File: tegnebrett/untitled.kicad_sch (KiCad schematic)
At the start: 39 parts, among them U1 XC7A100T-2FTG256I

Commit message: feat: add FPGA footprint and add footprint to PCB
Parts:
- U1: footprint (none) -> tegnebrett_modules:fpga
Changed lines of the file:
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@@
 			)
 		)
-		(property "Footprint" ""
+		(property "Footprint" "tegnebrett_modules:fpga"
 			(at 204.47 85.09 0)
 			(effects

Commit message: feat: add footprint for each capacitor
It's all 0805, 1206 or 1210 hand soldering variants.
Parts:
- C1, C10, C11, C12, C13, C15, C16, C17, C18, C19, C21, C22, C23, C24, C26, C27, C28, C29, C3, C31, C32, C33, C34, C36, C37, C38, C39, C40, C41, C42, C43, C44, C45, C5, C7, C9: footprint (none) -> Capacitor_SMD:C_0805_2012Metric_Pad1.18x1.45mm_HandSolder
- C4: footprint (none) -> Capacitor_SMD:C_1210_3225Metric_Pad1.33x2.70mm_HandSolder
- C6: footprint (none) -> Capacitor_SMD:C_1206_3216Metric_Pad1.33x1.80mm_HandSolder
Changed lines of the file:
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@@
 			)
 		)
-		(property "Footprint" ""
+		(property "Footprint" "Capacitor_SMD:C_0805_2012Metric_Pad1.18x1.45mm_HandSolder"
 			(at 38.4048 86.36 0)
 			(effects
@@
 			)
 		)
-		(property "Footprint" ""
+		(property "Footprint" "Capacitor_SMD:C_0805_2012Metric_Pad1.18x1.45mm_HandSolder"
 			(at 59.3852 62.23 0)
 			(effects
@@
 			)
 		)
-		(property "Footprint" ""
+		(property "Footprint" "Capacitor_SMD:C_0805_2012Metric_Pad1.18x1.45mm_HandSolder"
 			(at 33.9852 36.83 0)
 			(effects
@@
 			)
 		)
-		(property "Footprint" ""
+		(property "Footprint" "Capacitor_SMD:C_0805_2012Metric_Pad1.18x1.45mm_HandSolder"
 			(at 53.0352 62.23 0)
 			(effects
@@
 			)
 		)
-		(property "Footprint" ""
+		(property "Footprint" "Capacitor_SMD:C_0805_2012Metric_Pad1.18x1.45mm_HandSolder"
 			(at 57.4548 86.36 0)
 			(effects
@@
 			)
 		)
-		(property "Footprint" ""
+		(property "Footprint" "Capacitor_SMD:C_0805_2012Metric_Pad1.18x1.45mm_HandSolder"
 			(at 40.3352 36.83 0)
 			(effects
@@
 			)
 		)
-		(property "Footprint" ""
+		(property "Footprint" "Capacitor_SMD:C_0805_2012Metric_Pad1.18x1.45mm_HandSolder"
 			(at 101.9048 86.36 0)
 			(effects
@@
 			)
 		)
-		(property "Footprint" ""
+		(property "Footprint" "Capacitor_SMD:C_0805_2012Metric_Pad1.18x1.45mm_HandSolder"
 			(at 33.9852 62.23 0)
 			(effects
@@
 			)
 		)
-		(property "Footprint" ""
+		(property "Footprint" "Capacitor_SMD:C_0805_2012Metric_Pad1.18x1.45mm_HandSolder"
 			(at 65.7352 62.23 0)
 			(effects
@@
 			)
 		)
-		(property "Footprint" ""
+		(property "Footprint" "Capacitor_SMD:C_0805_2012Metric_Pad1.18x1.45mm_HandSolder"
 			(at 89.2048 86.36 0)
 			(effects
@@
 			)
 		)
-		(property "Footprint" ""
+		(property "Footprint" "Capacitor_SMD:C_0805_2012Metric_Pad1.18x1.45mm_HandSolder"
 			(at 70.1548 86.36 0)
 			(effects
@@
 			)
 		)
-		(property "Footprint" ""
+		(property "Footprint" "Capacitor_SMD:C_0805_2012Metric_Pad1.18x1.45mm_HandSolder"
 			(at 51.1048 86.36 0)
 			(effects
@@
 			)
 		)
-		(property "Footprint" ""
+		(property "Footprint" "Capacitor_SMD:C_0805_2012Metric_Pad1.18x1.45mm_HandSolder"
 			(at 40.3352 113.03 0)
 			(effects
@@
 			)
 		)
-		(property "Footprint" ""
+		(property "Footprint" "Capacitor_SMD:C_0805_2012Metric_Pad1.18x1.45mm_HandSolder"
 			(at 63.8048 86.36 0)
 			(effects
@@
 			)
 		)
-		(property "Footprint" ""
+		(property "Footprint" "Capacitor_SMD:C_0805_2012Metric_Pad1.18x1.45mm_HandSolder"
 			(at 40.3352 62.23 0)
 			(effects
@@
 			)
 		)
-		(property "Footprint" ""
+		(property "Footprint" "Capacitor_SMD:C_1206_3216Metric_Pad1.33x1.80mm_HandSolder"
 			(at 27.6352 135.89 0)
 			(effects
@@
 			)
 		)
-		(property "Footprint" ""
+		(property "Footprint" "Capacitor_SMD:C_0805_2012Metric_Pad1.18x1.45mm_HandSolder"
 			(at 53.0352 113.03 0)
 			(effects
@@
 			)
 		)
-		(property "Footprint" ""
+		(property "Footprint" "Capacitor_SMD:C_0805_2012Metric_Pad1.18x1.45mm_HandSolder"
 			(at 82.8548 86.36 0)
 			(effects
@@
 			)
 		)
-		(property "Footprint" ""
+		(property "Footprint" "Capacitor_SMD:C_0805_2012Metric_Pad1.18x1.45mm_HandSolder"
 			(at 95.5548 86.36 0)
 			(effects
@@
 			)
 		)
-		(property "Footprint" ""
+		(property "Footprint" "Capacitor_SMD:C_0805_2012Metric_Pad1.18x1.45mm_HandSolder"
 			(at 33.9852 135.89 0)
 			(effects
@@
 			)
 		)
-		(property "Footprint" ""
+		(property "Footprint" "Capacitor_SMD:C_0805_2012Metric_Pad1.18x1.45mm_HandSolder"
 			(at 59.3852 36.83 0)
 			(effects
@@
 			)
 		)
-		(property "Footprint" ""
+		(property "Footprint" "Capacitor_SMD:C_0805_2012Metric_Pad1.18x1.45mm_HandSolder"
 			(at 46.6852 36.83 0)
 			(effects
@@
 			)
 		)
-		(property "Footprint" ""
+		(property "Footprint" "Capacitor_SMD:C_0805_2012Metric_Pad1.18x1.45mm_HandSolder"
 			(at 53.0352 36.83 0)
 			(effects
@@
 			)
 		)
-		(property "Footprint" ""
+		(property "Footprint" "Capacitor_SMD:C_1210_3225Metric_Pad1.33x2.70mm_HandSolder"
 			(at 25.7048 86.36 0)
 			(effects
@@
 			)
 		)
-		(property "Footprint" ""
+		(property "Footprint" "Capacitor_SMD:C_0805_2012Metric_Pad1.18x1.45mm_HandSolder"
 			(at 65.7352 36.83 0)
 			(effects
@@
 			)
 		)
-		(property "Footprint" ""
+		(property "Footprint" "Capacitor_SMD:C_0805_2012Metric_Pad1.18x1.45mm_HandSolder"
 			(at 114.6048 86.36 0)
 			(effects
@@
 			)
 		)
-		(property "Footprint" ""
+		(property "Footprint" "Capacitor_SMD:C_0805_2012Metric_Pad1.18x1.45mm_HandSolder"
 			(at 27.6352 62.23 0)
 			(effects
@@
 			)
 		)
-		(property "Footprint" ""
+		(property "Footprint" "Capacitor_SMD:C_0805_2012Metric_Pad1.18x1.45mm_HandSolder"
 			(at 59.3852 113.03 0)
 			(effects
@@
 			)
 		)
-		(property "Footprint" ""
+		(property "Footprint" "Capacitor_SMD:C_0805_2012Metric_Pad1.18x1.45mm_HandSolder"
 			(at 27.6352 36.83 0)
 			(effects
@@
 			)
 		)
-		(property "Footprint" ""
+		(property "Footprint" "Capacitor_SMD:C_0805_2012Metric_Pad1.18x1.45mm_HandSolder"
 			(at 27.6352 113.03 0)
 			(effects
@@
 			)
 		)
-		(property "Footprint" ""
+		(property "Footprint" "Capacitor_SMD:C_0805_2012Metric_Pad1.18x1.45mm_HandSolder"
 			(at 44.7548 86.36 0)
 			(effects
@@
 			)
 		)
-		(property "Footprint" ""
+		(property "Footprint" "Capacitor_SMD:C_0805_2012Metric_Pad1.18x1.45mm_HandSolder"
 			(at 76.5048 86.36 0)
 			(effects
@@
 			)
 		)
-		(property "Footprint" ""
+		(property "Footprint" "Capacitor_SMD:C_0805_2012Metric_Pad1.18x1.45mm_HandSolder"
 			(at 40.3352 135.89 0)
 			(effects
@@
 			)
 		)
-		(property "Footprint" ""
+		(property "Footprint" "Capacitor_SMD:C_0805_2012Metric_Pad1.18x1.45mm_HandSolder"
 			(at 33.9852 113.03 0)
 			(effects
@@
 			)
 		)
-		(property "Footprint" ""
+		(property "Footprint" "Capacitor_SMD:C_0805_2012Metric_Pad1.18x1.45mm_HandSolder"
 			(at 46.6852 62.23 0)
 			(effects
@@
 			)
 		)
-		(property "Footprint" ""
+		(property "Footprint" "Capacitor_SMD:C_0805_2012Metric_Pad1.18x1.45mm_HandSolder"
 			(at 32.0548 86.36 0)
 			(effects
@@
 			)
 		)
-		(property "Footprint" ""
+		(property "Footprint" "Capacitor_SMD:C_0805_2012Metric_Pad1.18x1.45mm_HandSolder"
 			(at 46.6852 113.03 0)
 			(effects
@@
 			)
 		)
-		(property "Footprint" ""
+		(property "Footprint" "Capacitor_SMD:C_0805_2012Metric_Pad1.18x1.45mm_HandSolder"
 			(at 108.2548 86.36 0)
 			(effects

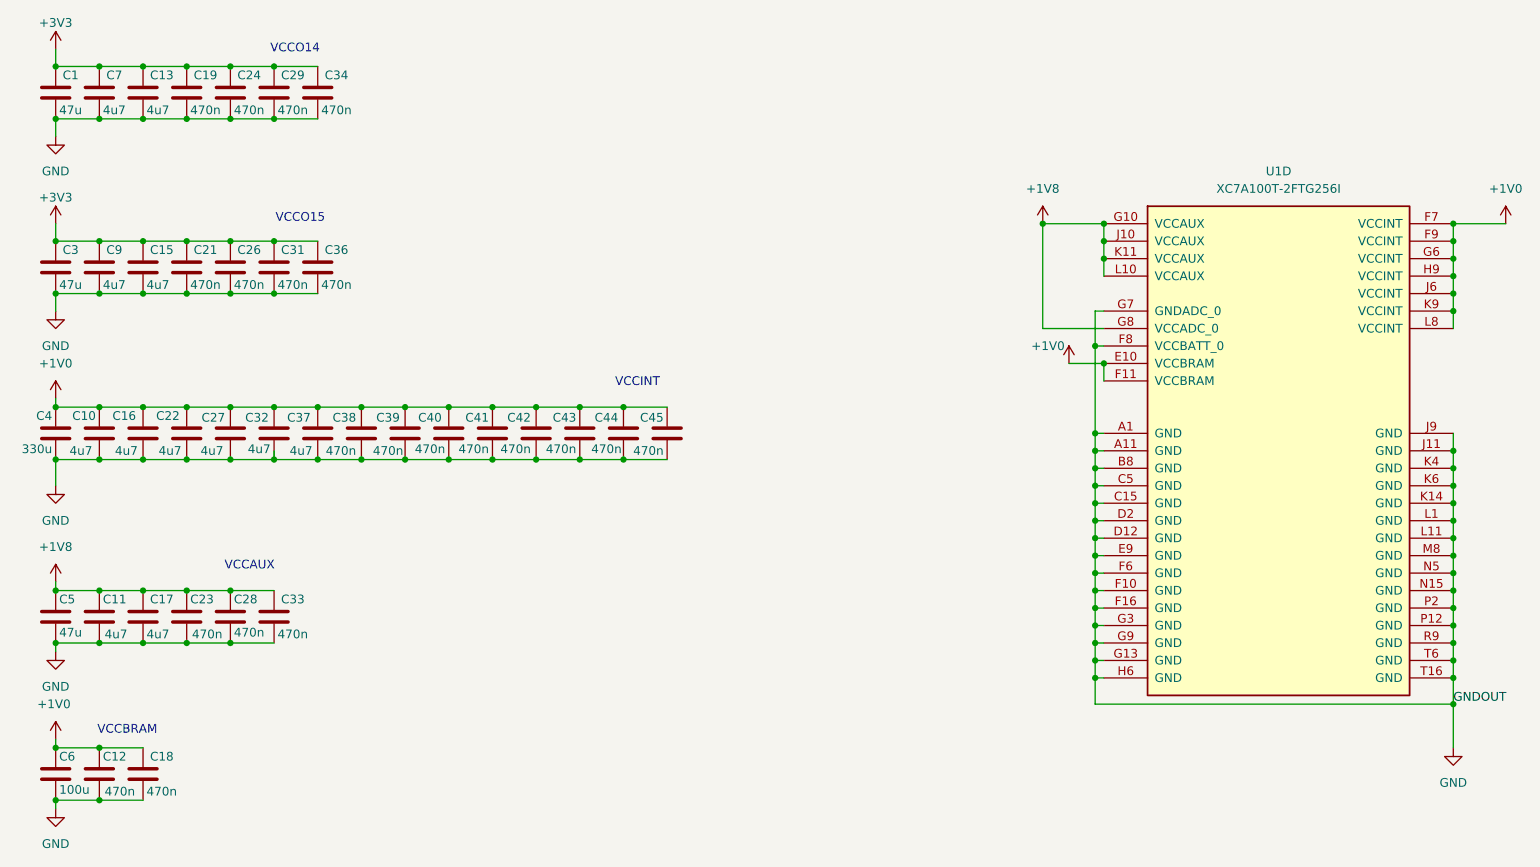
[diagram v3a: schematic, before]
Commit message: refactor: re-annotate schematic labels
References for schematic capacitors (for example C74 -> C2), etc.
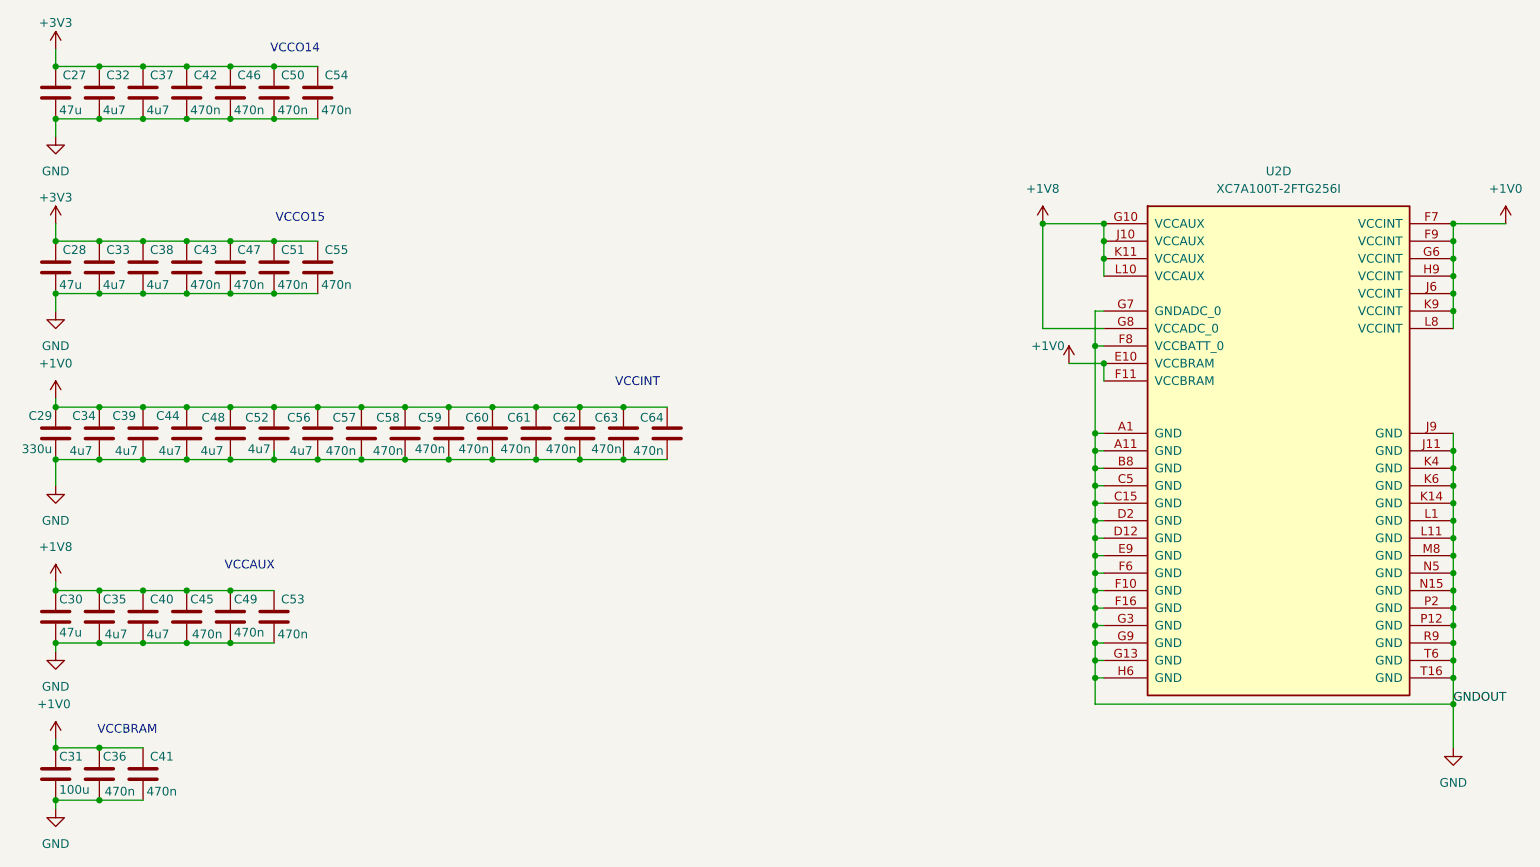
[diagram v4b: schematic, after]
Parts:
- renumbered C1 to C27, C3 to C28, C4 to C29, C5 to C30, C6 to C31, C7 to C32, C9 to C33, C10 to C34, C11 to C35, C12 to C36, C13 to C37, C15 to C38, C16 to C39, C17 to C40, C18 to C41, C19 to C42, C21 to C43, C22 to C44, C23 to C45, C24 to C46, C26 to C47, C27 to C48, C28 to C49, C29 to C50, C31 to C51, C32 to C52, C33 to C53, C34 to C54, C36 to C55, C37 to C56, C38 to C57, C39 to C58, C40 to C59, C41 to C60, C42 to C61, C43 to C62, C44 to C63, C45 to C64, U1 to U2
